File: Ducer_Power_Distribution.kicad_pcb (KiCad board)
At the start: 2 copper layers, 115 x 67 mm, 16 parts, among them J1 Mini_Fit_Jr_1x3_pin, J10 Conn_01x05, J11 Power In, J2 Mini_Fit_Jr_1x3_pin, J3 Mini_Fit_Jr_1x3_pin, J4 Mini_Fit_Jr_1x3_pin, J5 Mini_Fit_Jr_1x3_pin, J6 Mini_Fit_Jr_1x3_pin, J7 Mini_Fit_Jr_1x3_pin, J8 Mini_Fit_Jr_1x3_pin, J9 Conn_01x05

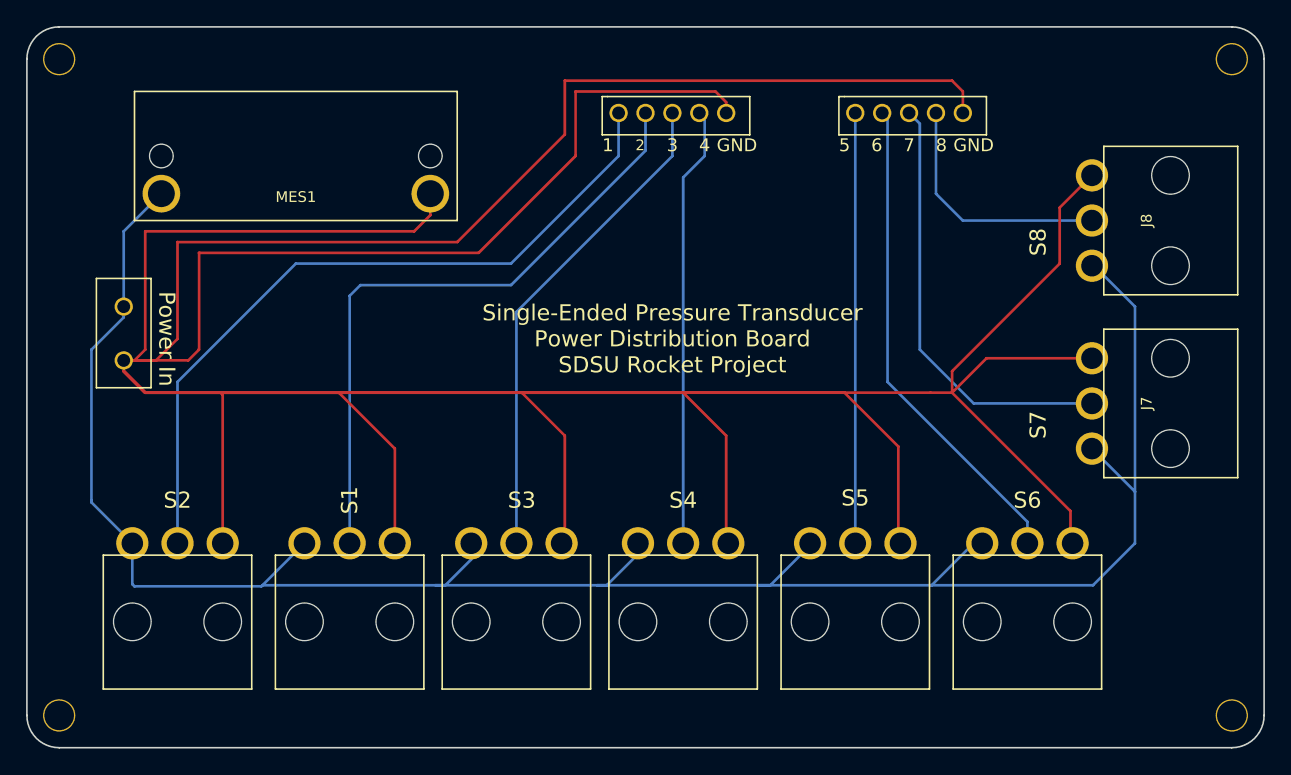
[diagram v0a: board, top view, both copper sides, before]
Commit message: Made routes 0.75mmthick
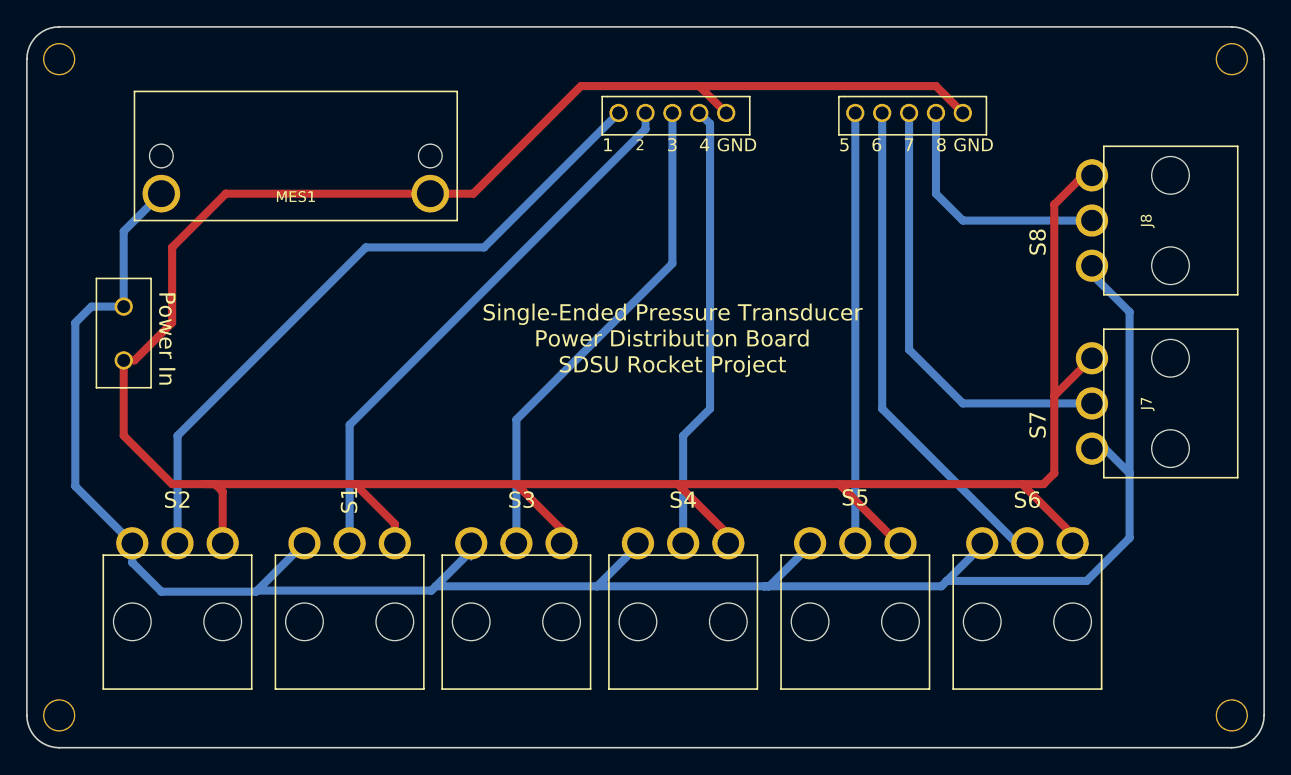
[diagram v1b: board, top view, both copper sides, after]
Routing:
- net GND: track 622.9 -> 272.8 mm
- net Net-(J2-Pad2): track 59.6 -> 51.4 mm
- net Net-(J1-Pad2): track 68.7 -> 63.4 mm
- net VCC: track 202.5 -> 204.0 mm
- net Net-(J10-Pad2): track 45.6 -> 46.9 mm
- net Net-(J4-Pad2): track 41.0 -> 42.2 mm
- net Net-(J10-Pad3): track 40.5 -> 41.1 mm
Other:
- net class Default: trace_width 0.25 -> 0.75

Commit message: added copper pour zones
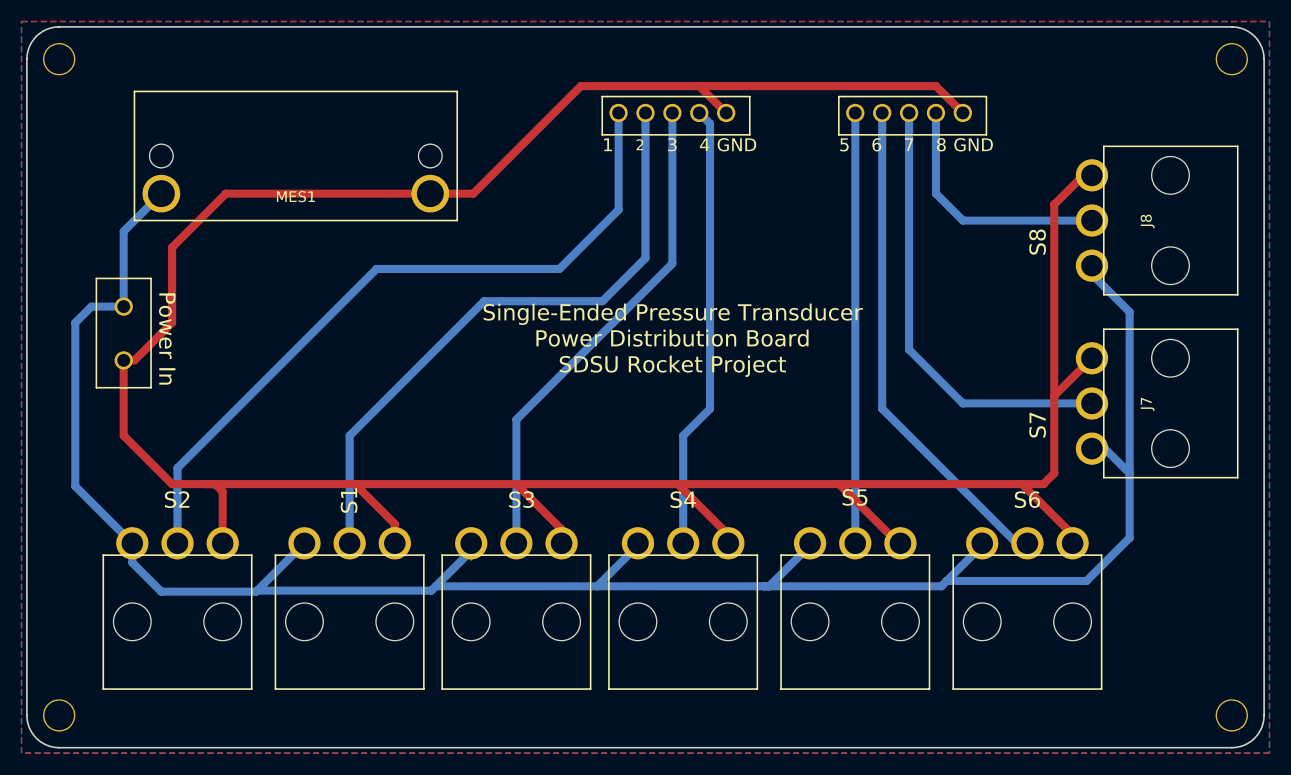
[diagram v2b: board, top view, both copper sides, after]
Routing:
- net Net-(J2-Pad2): track 51.4 -> 58.8 mm
- net Net-(J1-Pad2): track 63.4 -> 66.9 mm
- added copper zone on B.Cu, net GND
- added copper zone on F.Cu, net GND
